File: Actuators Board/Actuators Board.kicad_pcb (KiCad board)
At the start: 2 copper layers, 89 parts, among them IC1 BD62120AEFJ-E2, J10 Conn_01x02_Male, J3 USB_C_Receptacle_USB2.0, J4 Conn_01x03_Male, J5 Conn_01x06_Male, J9 Conn_01x02_Male, Q1 MMDT2222A, Q2 SI2366DS, U1 ESP32-PICO-D4, U2 TPS54233D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

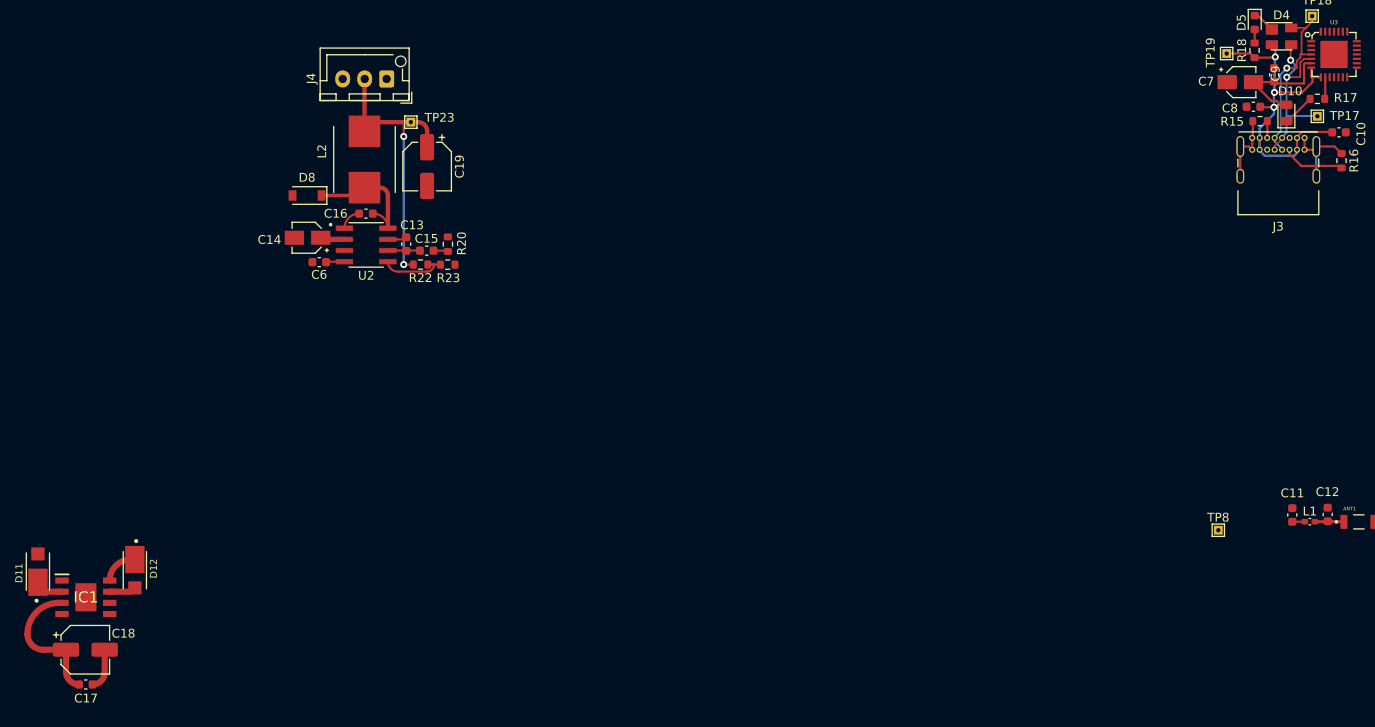
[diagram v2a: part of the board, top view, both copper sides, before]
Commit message: Annotated schematic and imported changes into PCB
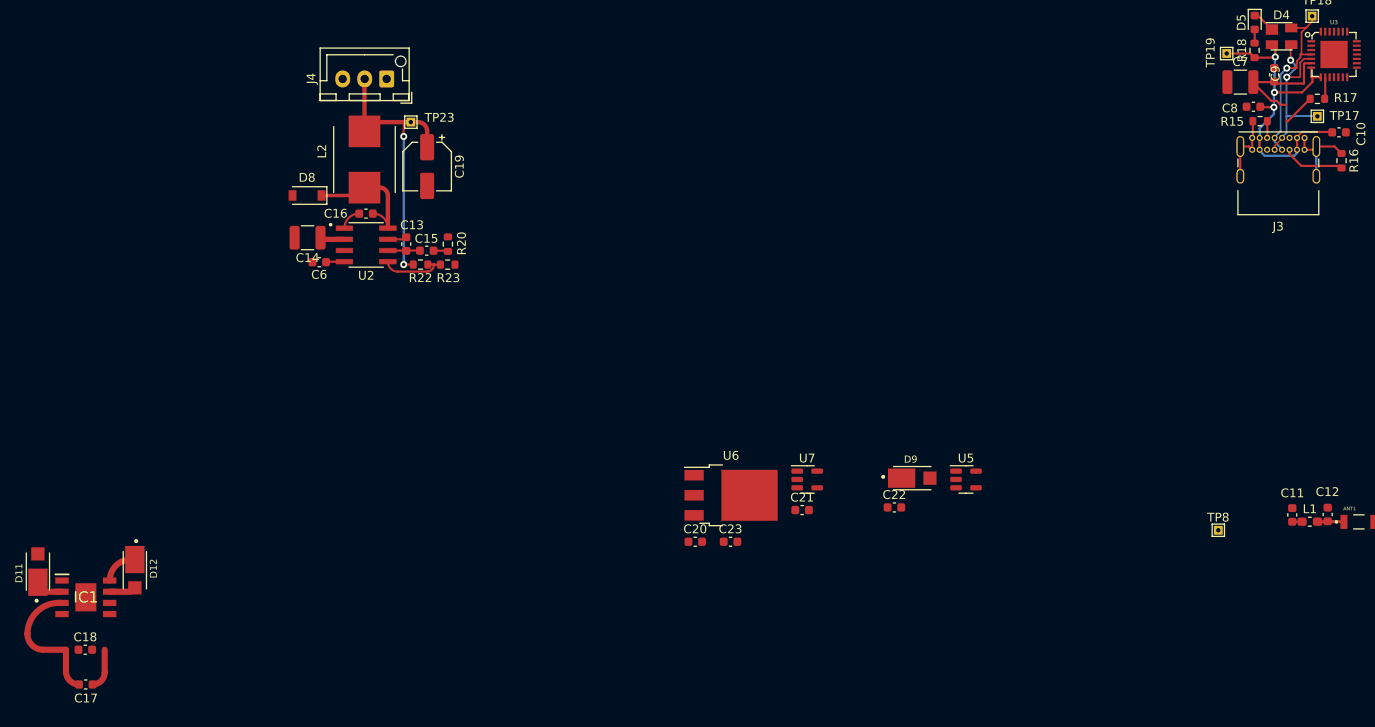
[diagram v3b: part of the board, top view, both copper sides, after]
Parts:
- removed D10: D_Small, Diode_SMD:D_0805_2012Metric
- added C20: 10uF, Capacitor_SMD:C_0603_1608Metric, F.Cu at (143.2, 90.1)
- added C21: 22uF, Capacitor_SMD:C_0603_1608Metric, F.Cu at (155.4, 86.5)
- added C22: 4.7uF, Capacitor_SMD:C_0603_1608Metric, F.Cu at (165.9, 86.2)
- added C23: 4.7uF, Capacitor_SMD:C_0603_1608Metric, F.Cu at (147.2, 90.1)
- added D9: V8PAM10S, iclr:DIO_V3PAN50-M3_I, F.Cu at (167.9, 82.9)
- added U5: LTC4411, Package_TO_SOT_SMD:SOT-23-5, F.Cu at (174.0, 83.0)
- added U6: AZ1084-3.3, Package_TO_SOT_SMD:TO-252-3_TabPin2, F.Cu at (147.3, 84.8)
- added U7: LTC4411, Package_TO_SOT_SMD:SOT-23-5, F.Cu at (155.9, 83.0)
- C14: footprint Capacitor_SMD:CP_Elec_3x5.3 -> Capacitor_SMD:C_1210_3225Metric
- C18: value 100uF -> 4.7uF; footprint Capacitor_SMD:CP_Elec_5x5.9 -> Capacitor_SMD:C_0603_1608Metric
- C7: value 4.7uF -> 10uF; footprint Capacitor_SMD:CP_Elec_3x5.3 -> Capacitor_SMD:C_1210_3225Metric
- D11, D12: value V3PAN50-M3/I -> V8PAM10S
- L1: footprint Inductor_SMD:L_0402_1005Metric_Pad0.77x0.64mm_HandSolder -> Inductor_SMD:L_0603_1608Metric_Pad1.05x0.95mm_HandSolder
- R12: value 1k -> 10k
- R3: value 470 -> 24k
- R4: value 470 -> 3.5k
- R6: value 1k -> 47k
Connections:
- C10 pad 2: VBUS -> +3V3
- C18 pad 1: +24V -> GND
- C18 pad 2: GND -> +3V3
- C7 pad 1: GND -> +24V
- C7 pad 2: Net-(C7-Pad2) -> GND
- C8 pad 2: VBUS -> +3V3
- C9 pad 2: Net-(C7-Pad2) -> +3V3
- Q2 pad 1: /SolEN -> Net-(Q2-Pad1)
- R12 pad 1: +24V -> /SolEN
- R12 pad 2: Net-(R12-Pad2) -> GND
- R21 pad 1: /SolEN -> Net-(Q2-Pad1)
- R21 pad 2: GND -> /SolEN
- R3 pad 1: Net-(R3-Pad1) -> VBUS
- R3 pad 2: GND -> (no net)
- R4 pad 1: Net-(R3-Pad1) -> +24V
- R6 pad 1: Net-(R12-Pad2) -> GND
- R6 pad 2: Net-(R3-Pad1) -> Net-(R3-Pad2)
- U3 pad 6: Net-(C7-Pad2) -> +3V3
- U3 pad 7: VBUS -> +3V3
- U3 pad 8: VBUS -> Net-(R3-Pad2)
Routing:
- net +3V3: track 45.2 -> 59.0 mm
- net Net-(C7-Pad2): track 13.8 -> 0.00 mm
- net Net-(R3-Pad1): track 3.04 -> 0.00 mm
- net VBUS: track 40.2 -> 43.2 mm
- net GND: track 31.9 -> 34.3 mm
- net Net-(R12-Pad2): track 2.36 -> 0.00 mm

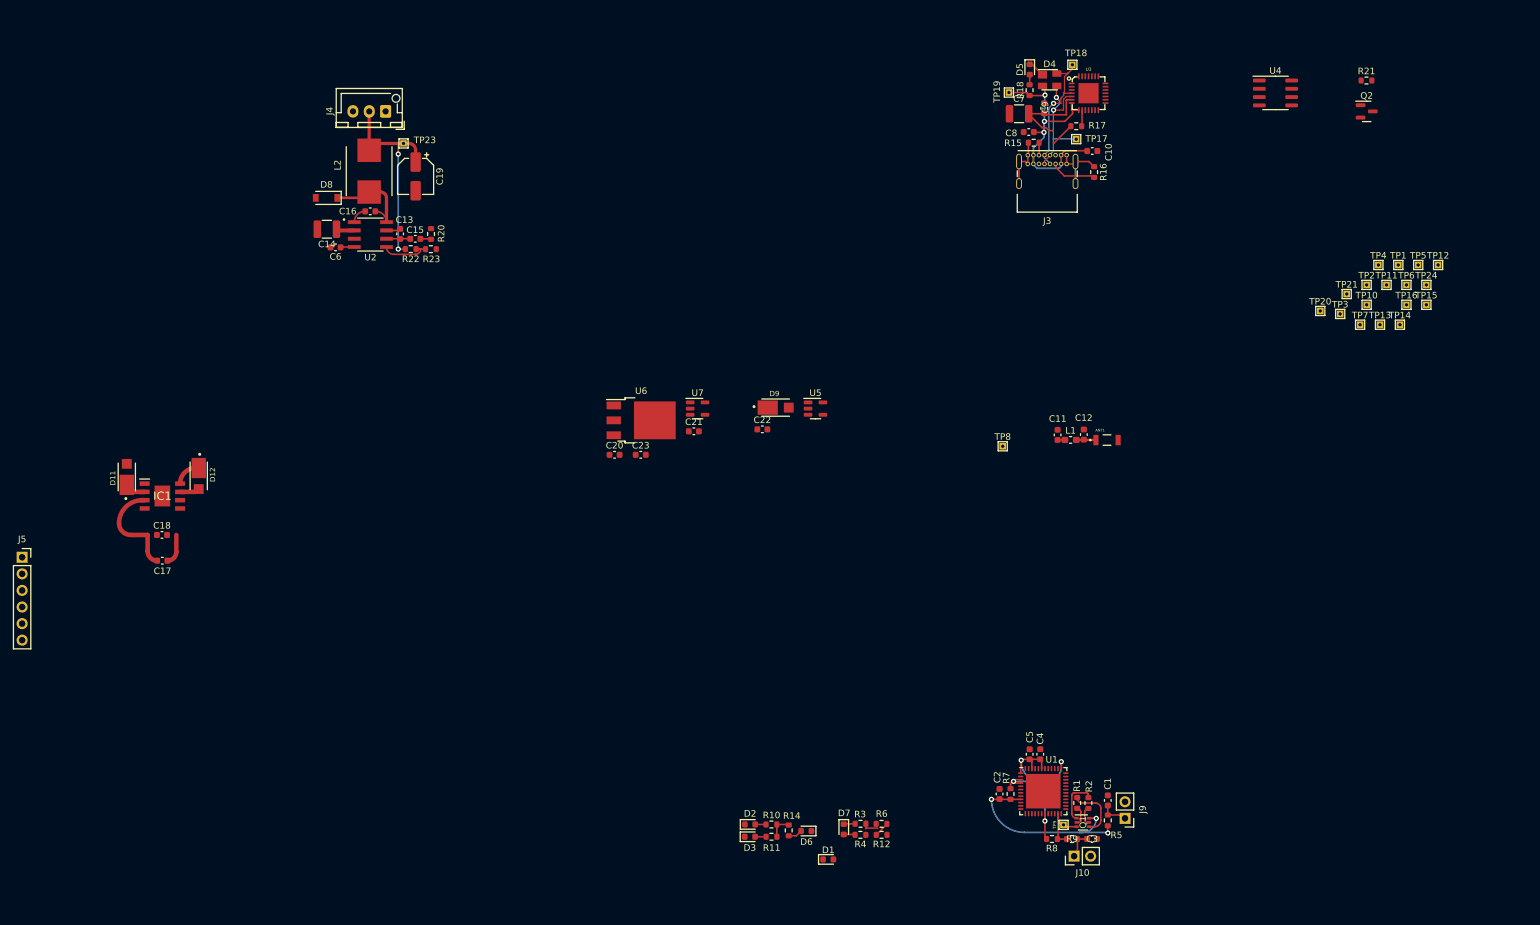
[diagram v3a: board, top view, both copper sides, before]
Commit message: H bridge & CAN Transceiver final placement
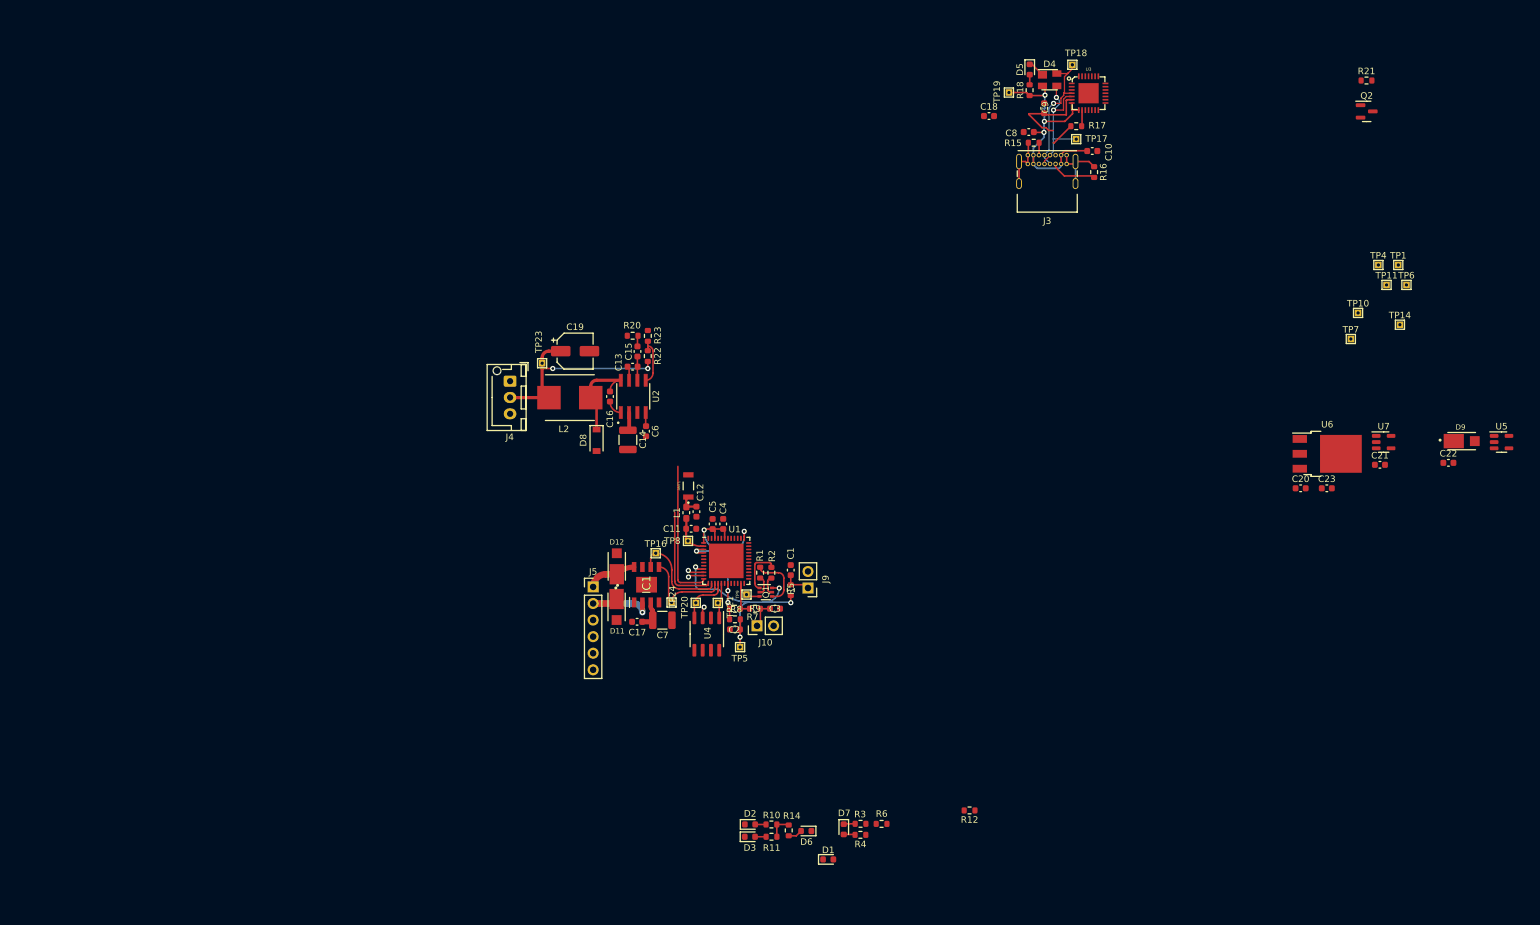
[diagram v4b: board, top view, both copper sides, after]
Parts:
- removed TP12, TP13, TP15, TP2, TP3: TestPoint, TestPoint:TestPoint_THTPad_1.0x1.0mm_Drill0.5mm
- J5: footprint Connector_PinSocket_2.54mm:PinSocket_1x06_P2.54mm_Vertical -> Connector_PinHeader_2.54mm:PinHeader_1x06_P2.54mm_Vertical
- moved C18 142.0 mm to (200.6, 38.2)
- moved TP24 125.5 mm to (152.0, 112.8)
- moved TP16 121.1 mm to (149.5, 105.2)
- moved U4 120.3 mm to (157.4, 117.6), turned to -90 degrees
- moved TP5 119.2 mm to (162.5, 119.6)
- moved TP21 107.3 mm to (159.1, 112.8)
- moved TP20 105.6 mm to (155.7, 112.8)
- moved C20 105.2 mm to (248.3, 95.3)
- moved U5 105.2 mm to (279.1, 88.2)
- moved U7 105.2 mm to (261.1, 88.2)
- moved C21 105.2 mm to (260.5, 91.7)
- moved C22 105.2 mm to (271.0, 91.4)
- moved C23 105.2 mm to (252.3, 95.3)
- moved D9 105.2 mm to (273.0, 88.0)
- moved U6 105.2 mm to (252.4, 90.0)
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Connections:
- C21 pad 2: (no net) -> Net-(C21-Pad2)
- R3 pad 2: (no net) -> Net-(R3-Pad2)
- U1 pad 10: unconnected-(U1-Pad10) -> /Hall1
- U1 pad 11: unconnected-(U1-Pad11) -> /Hall2
- U1 pad 12: /CAN_TX -> /SolEN
- U1 pad 13: /CAN_RX -> /ServoPWM
- U1 pad 14: unconnected-(U1-Pad14) -> /HBridgeDIR2
- U1 pad 16: /HBridgeDIR2 -> /CAN_RX
- U1 pad 17: /ServoPWM -> /CAN_TX
- U1 pad 21: /SolEN -> unconnected-(U1-Pad21)
- U1 pad 24: /Hall2 -> unconnected-(U1-Pad24)
- U1 pad 34: /Hall1 -> unconnected-(U1-Pad34)
- U5 pad 1: (no net) -> Net-(J1-Pad4)
- U5 pad 4: (no net) -> unconnected-(U5-Pad4)
- U7 pad 4: (no net) -> unconnected-(U7-Pad4)
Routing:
- net /SolEN: track 0.00 -> 21.8 mm
- net /ServoPWM: track 0.00 -> 16.2 mm
- net /HBridgeDIR2: track 0.00 -> 15.5 mm
- net /HBridgeDIR1: track 0.00 -> 15.0 mm
- net +24V: track 18.6 -> 7.81 mm
- net /Motor-: track 3.14 -> 13.7 mm, vias 0 -> 1
- net GND: track 34.3 -> 24.2 mm
- net /CAN_RX: track 0.00 -> 8.01 mm
- net /CAN_TX: track 0.00 -> 5.69 mm
- net /EN: track 31.0 -> 36.0 mm, vias 3 -> 4
- net /LNA_IN: track 1.44 -> 6.27 mm
- net /Motor+: track 4.12 -> 7.59 mm
- net VBUS: track 43.2 -> 40.2 mm
- net /Hall1: track 0.00 -> 2.51 mm, vias 0 -> 1
- net /Hall2: track 0.00 -> 2.46 mm, vias 0 -> 1
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
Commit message: Buck converter placement & merged USB layout from 2nd board
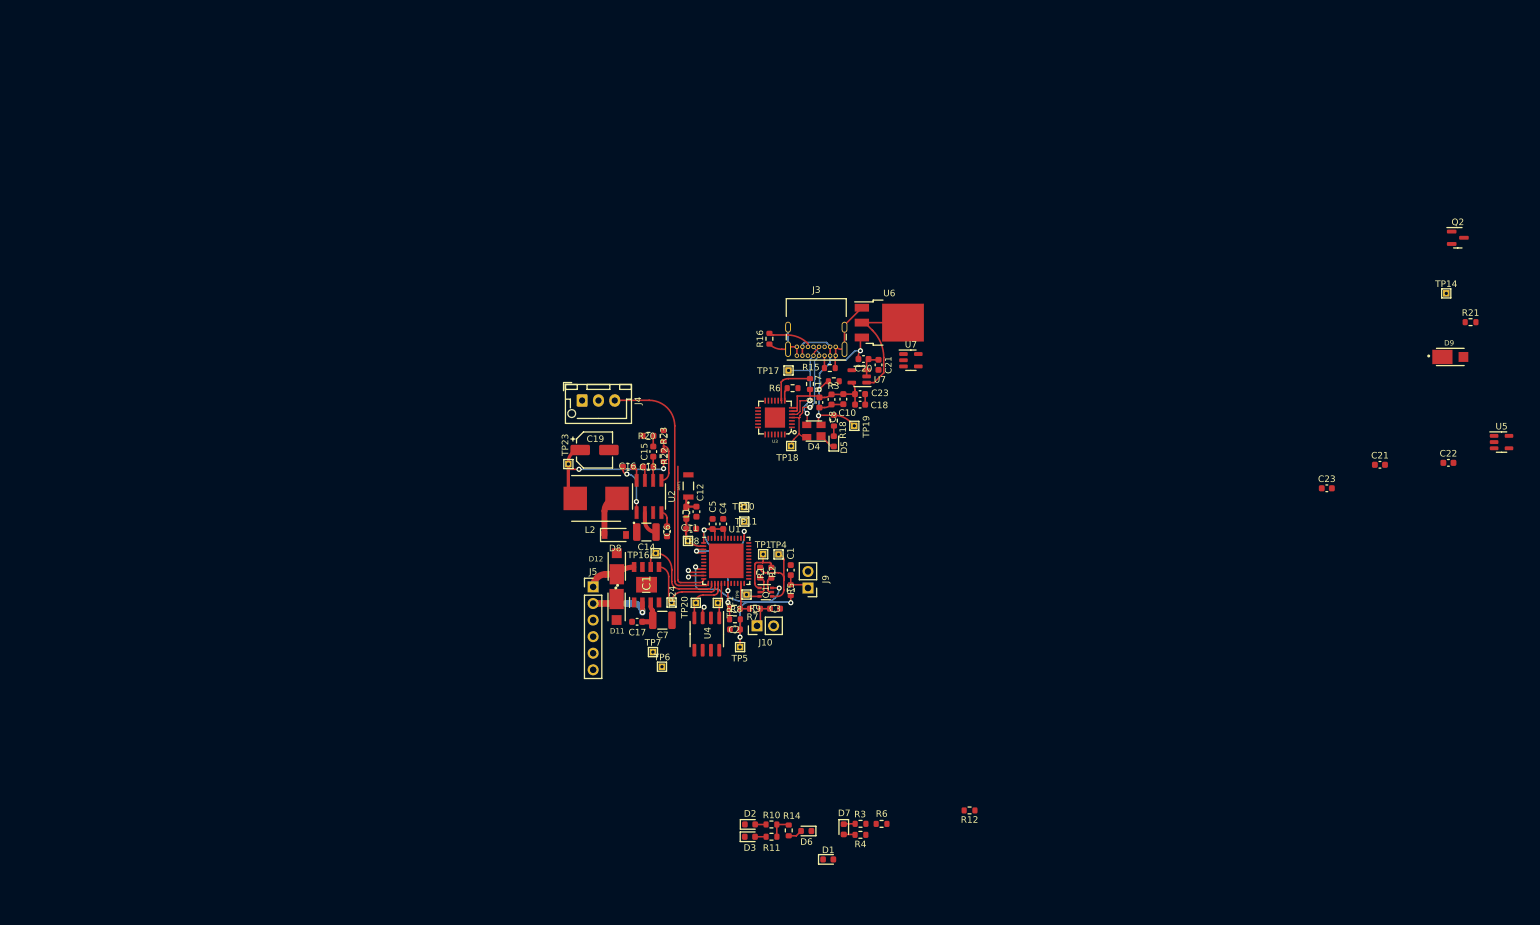
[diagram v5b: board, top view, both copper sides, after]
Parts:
- added C21: 22uF, Capacitor_SMD:C_0603_1608Metric, F.Cu at (183.7, 76.3)
- added C23: 4.7uF, Capacitor_SMD:C_0603_1608Metric, F.Cu at (180.8, 80.8)
- added R3: 24k, Resistor_SMD:R_0603_1608Metric, F.Cu at (176.8, 78.9)
- added R6: 47k, Resistor_SMD:R_0603_1608Metric, F.Cu at (170.5, 79.9)
- added U7: LTC4411, Package_TO_SOT_SMD:SOT-23-5, F.Cu at (180.7, 78.1)
- moved TP6 128.2 mm to (150.5, 122.6)
- moved TP7 117.2 mm to (149.1, 120.3)
- moved TP1 106.9 mm to (166.0, 105.4)
- moved TP11 104.9 mm to (163.1, 100.4)
- moved TP4 102.0 mm to (168.3, 105.4)
- moved TP10 98.6 mm to (163.1, 98.1)
- moved U7 73.5 mm to (188.6, 75.6)
- moved TP18 72.6 mm to (170.3, 88.8), turned to 180 degrees
- moved U6 70.0 mm to (185.3, 69.9)
- moved C20 69.8 mm to (181.4, 75.5), turned to 180 degrees
- moved U3 69.1 mm to (167.8, 84.4), turned to 180 degrees
- moved D4 64.8 mm to (173.8, 86.5), turned to 180 degrees
- moved D5 64.4 mm to (176.8, 88.1), turned to 90 degrees
- moved R18 58.8 mm to (176.8, 84.9), turned to -90 degrees
- moved R17 56.8 mm to (173.2, 79.3), turned to 90 degrees
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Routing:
- net /ServoPWM: track 16.2 -> 40.7 mm
- net Net-(C21-Pad2): track 0.00 -> 18.6 mm
- net GND: track 24.2 -> 38.0 mm
- net +6V: track 33.4 -> 24.7 mm
- net Net-(C16-Pad1): track 2.55 -> 8.10 mm, vias 0 -> 2
- net Net-(R17-Pad2): track 2.49 -> 7.44 mm
- net Net-(C16-Pad2): track 14.8 -> 10.3 mm
- net /DTR: track 8.69 -> 13.0 mm
- net VBUS: track 40.2 -> 38.2 mm
- net Net-(R3-Pad2): track 0.00 -> 1.73 mm
- net /RTS: track 7.27 -> 8.59 mm
- net +24V: track 7.81 -> 8.92 mm
- net /USB -> UART/Data-: track 21.6 -> 21.0 mm
- net /USB -> UART/Data+: track 20.9 -> 20.4 mm
